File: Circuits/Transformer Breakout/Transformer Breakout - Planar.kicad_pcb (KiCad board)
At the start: 2 copper layers, 17.8 x 30.5 mm, 2 parts, among them P1 XFRMR, P2 BRK

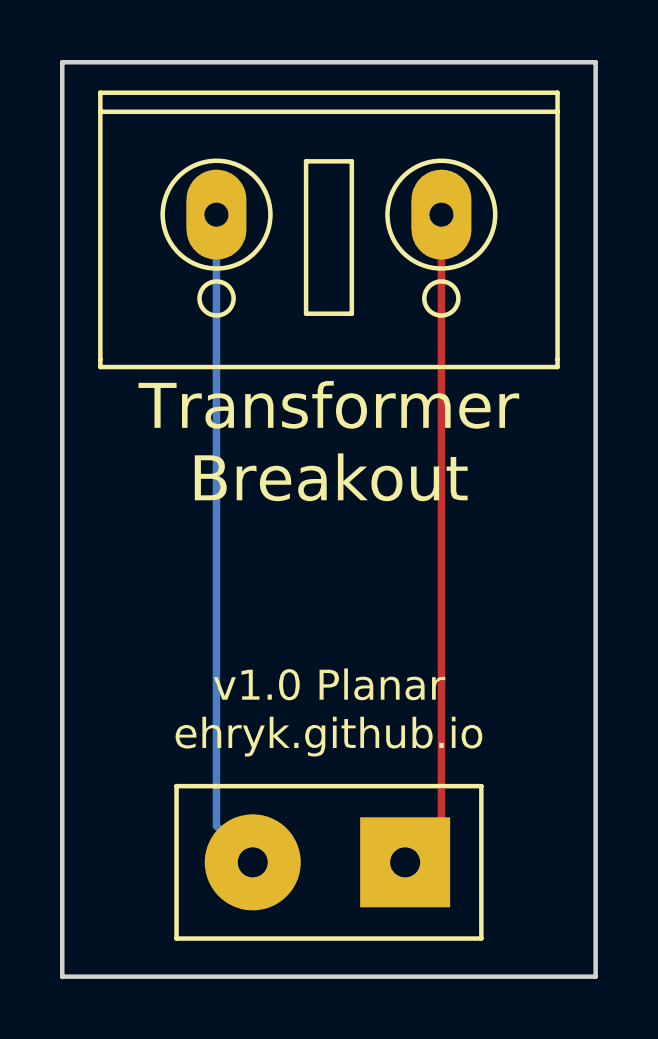
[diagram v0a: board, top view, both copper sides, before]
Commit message: Circuits: Small updates to Transformer Breakouts: circle icon, removing thermal rings
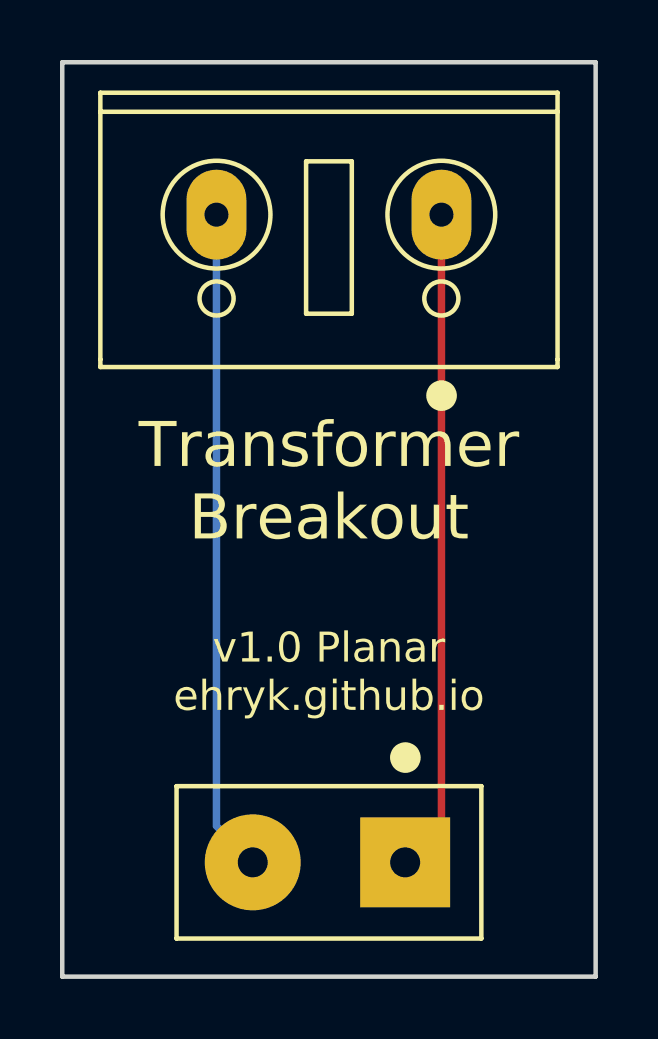
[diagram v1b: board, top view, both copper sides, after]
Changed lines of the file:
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@@
     (area 138.354999 83.744999 156.285001 114.375001)
     (thickness 1.6)
-    (drawings 8)
+    (drawings 12)
     (tracks 4)
     (zones 0)
@@
   (module Footprints:AMGIS_XFRMR (layer F.Cu)
     (at 147.32 110.49 180)
-    (fp_text reference P1 (at 0 3.81 180) (layer F.SilkS) hide
+    (fp_text reference P1 (at 6.35 -5.08 180) (layer F.Fab)
       (effects (font (size 1 1) (thickness 0.15)))
     )
-    (fp_text value XFRMR (at 0 3.81 180) (layer B.Fab) hide
-      (effects (font (size 1 1) (thickness 0.15)) (justify mirror))
+    (fp_text value XFRMR (at -5.08 -5.08 180) (layer F.Fab)
+      (effects (font (size 1 1) (thickness 0.15)))
     )
     (fp_line (start -5.08 -2.54) (end 5.08 -2.54) (layer B.SilkS) (width 0.15))
@@
   (module Footprints:ED110-2 (layer F.Cu)
     (at 147.32 88.9)
-    (fp_text reference P2 (at 5.08 6.35) (layer F.SilkS) hide
+    (fp_text reference P2 (at -6.35 -6.35) (layer F.Fab)
       (effects (font (size 1.2 1.2) (thickness 0.15)))
     )
-    (fp_text value BRK (at 0 6.35) (layer F.Fab) hide
+    (fp_text value BRK (at 5.08 -6.35) (layer F.Fab)
       (effects (font (size 1.2 1.2) (thickness 0.15)))
     )
@@
     (pad 2 thru_hole oval (at 3.75 0) (size 2 3) (drill 0.8) (layers *.Cu *.Mask)
       (net 1 /B))
+    (model "C:/Programming/KiCAD Parts/modules/packages3d/conn_mkds/mkds_1,5-2.wrl"
+      (at (xyz 0 -0.01 0))
+      (scale (xyz 1.5 0.9 1))
+      (rotate (xyz 0 0 180))
+    )
   )
-  (gr_text "v1.0 Planar\nehryk.github.io" (at 147.32 105.41) (layer F.SilkS)
-    (effects (font (size 1 1) (thickness 0.25)))
+  (gr_circle (center 149.86 106.9975) (end 149.919961 106.7435) (layer B.SilkS) (width 0.5))
+  (gr_circle (center 151.0665 94.9325) (end 151.126461 94.6785) (layer B.SilkS) (width 0.5))
+  (gr_circle (center 151.073481 94.9325) (end 151.133442 94.6785) (layer F.SilkS) (width 0.5))
+  (gr_circle (center 149.866981 106.9975) (end 149.926942 106.7435) (layer F.SilkS) (width 0.5))
+  (gr_text "v1.0 Planar\nehryk.github.io" (at 147.32 104.14) (layer F.SilkS)
+    (effects (font (size 1 1) (thickness 0.15)))
   )
-  (gr_text "Transformer\nBreakout" (at 147.32 96.52) (layer F.SilkS)
-    (effects (font (size 1.5 1.5) (thickness 0.3)))
+  (gr_text "Transformer\nBreakout" (at 147.32 97.79) (layer F.SilkS)
+    (effects (font (size 1.5 1.5) (thickness 0.25)))
   )
-  (gr_text "v1.0 Planar\nehryk.github.io" (at 147.32 105.41) (layer B.SilkS)
-    (effects (font (size 1 1) (thickness 0.25)) (justify mirror))
+  (gr_text "v1.0 Planar\nehryk.github.io" (at 147.32 104.14) (layer B.SilkS)
+    (effects (font (size 1 1) (thickness 0.15)) (justify mirror))
   )
-  (gr_text "Transformer\nBreakout" (at 147.32 96.52) (layer B.SilkS)
-    (effects (font (size 1.5 1.5) (thickness 0.3)) (justify mirror))
+  (gr_text "Transformer\nBreakout" (at 147.32 97.79) (layer B.SilkS)
+    (effects (font (size 1.5 1.5) (thickness 0.25)) (justify mirror))
   )
   (gr_line (start 138.43 114.3) (end 138.43 83.82) (angle 90) (layer Edge.Cuts) (width 0.15))
